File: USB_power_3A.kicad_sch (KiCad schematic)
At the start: 8 parts, among them J14 500SSP1S2M2QEA, J9 USB_C_Receptacle_PowerOnly_6P, U1 USBLC6-2SC6

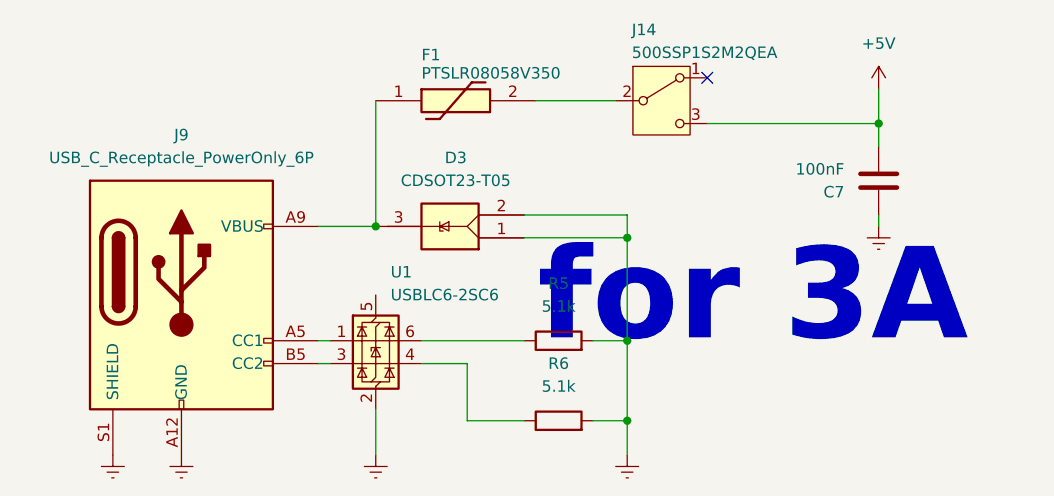
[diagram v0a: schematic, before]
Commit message: annotation and pcb outline
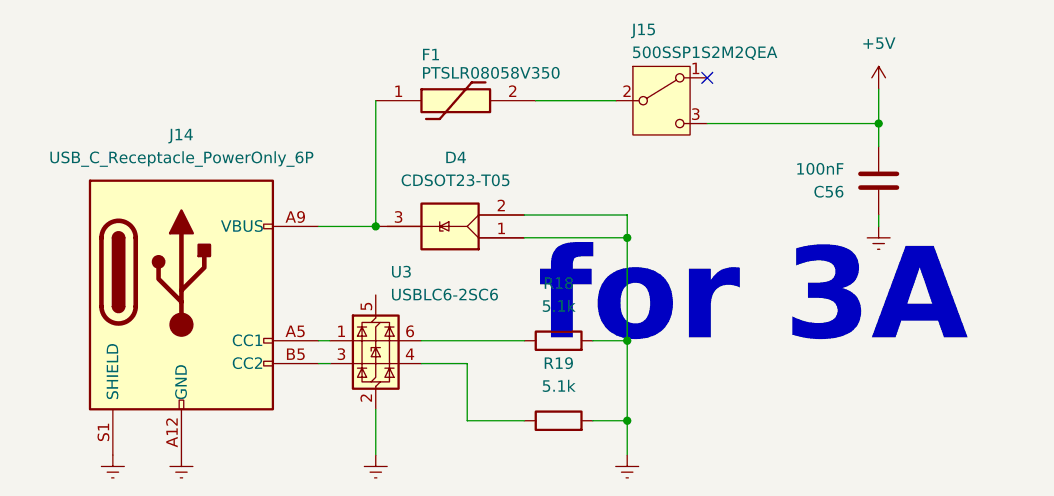
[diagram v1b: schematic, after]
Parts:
- renumbered C7 to C56, D3 to D4, J9 to J14, J14 to J15, R5 to R18, R6 to R19, U1 to U3
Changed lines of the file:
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@@
 		(on_board yes)
 		(dnp no)
-		(property "Reference" "J14"
+		(property "Reference" "J15"
 			(at 169.418 75.946 0)
 			(effects
@@
 			(project "RSC_extension_board"
 				(path "/1f48ed4c-84ce-4e77-88fc-25bf92dcee2d/a313b83a-a07e-4d1d-b36b-94744ea8af4d"
-					(reference "J14")
+					(reference "J15")
 					(unit 1)
 				)
@@
 		(dnp no)
 		(fields_autoplaced yes)
-		(property "Reference" "R6"
+		(property "Reference" "R19"
 			(at 161.29 113.03 90)
 			(effects
@@
 			(project "RSC_extension_board"
 				(path "/1f48ed4c-84ce-4e77-88fc-25bf92dcee2d/a313b83a-a07e-4d1d-b36b-94744ea8af4d"
-					(reference "R6")
+					(reference "R19")
 					(unit 1)
 				)
@@
 		(dnp no)
 		(fields_autoplaced yes)
-		(property "Reference" "#PWR026"
+		(property "Reference" "#PWR082"
 			(at 140.97 129.54 0)
 			(effects
@@
 			(project "RSC_extension_board"
 				(path "/1f48ed4c-84ce-4e77-88fc-25bf92dcee2d/a313b83a-a07e-4d1d-b36b-94744ea8af4d"
-					(reference "#PWR026")
+					(reference "#PWR082")
 					(unit 1)
 				)
@@
 		(dnp no)
 		(fields_autoplaced yes)
-		(property "Reference" "#PWR021"
+		(property "Reference" "#PWR084"
 			(at 196.85 86.36 0)
 			(effects
@@
 			(project "RSC_extension_board"
 				(path "/1f48ed4c-84ce-4e77-88fc-25bf92dcee2d/a313b83a-a07e-4d1d-b36b-94744ea8af4d"
-					(reference "#PWR021")
+					(reference "#PWR084")
 					(unit 1)
 				)
@@
 		(dnp no)
 		(fields_autoplaced yes)
-		(property "Reference" "#PWR74"
+		(property "Reference" "#PWR080"
 			(at 111.76 129.54 0)
 			(effects
@@
 			(project "RSC_extension_board"
 				(path "/1f48ed4c-84ce-4e77-88fc-25bf92dcee2d/a313b83a-a07e-4d1d-b36b-94744ea8af4d"
-					(reference "#PWR74")
+					(reference "#PWR080")
 					(unit 1)
 				)
@@
 		(dnp no)
 		(fields_autoplaced yes)
-		(property "Reference" "R5"
+		(property "Reference" "R18"
 			(at 161.29 104.14 90)
 			(effects
@@
 			(project "RSC_extension_board"
 				(path "/1f48ed4c-84ce-4e77-88fc-25bf92dcee2d/a313b83a-a07e-4d1d-b36b-94744ea8af4d"
-					(reference "R5")
+					(reference "R18")
 					(unit 1)
 				)
@@
 		(dnp no)
 		(fields_autoplaced yes)
-		(property "Reference" "C7"
+		(property "Reference" "C56"
 			(at 193.04 93.9801 0)
 			(effects
@@
 			(project "RSC_extension_board"
 				(path "/1f48ed4c-84ce-4e77-88fc-25bf92dcee2d/a313b83a-a07e-4d1d-b36b-94744ea8af4d"
-					(reference "C7")
+					(reference "C56")
 					(unit 1)
 				)
@@
 		(dnp no)
 		(fields_autoplaced yes)
-		(property "Reference" "U1"
+		(property "Reference" "U3"
 			(at 142.6211 102.87 0)
 			(effects
@@
 			(project "RSC_extension_board"
 				(path "/1f48ed4c-84ce-4e77-88fc-25bf92dcee2d/a313b83a-a07e-4d1d-b36b-94744ea8af4d"
-					(reference "U1")
+					(reference "U3")
 					(unit 1)
 				)
@@
 		(dnp no)
 		(fields_autoplaced yes)
-		(property "Reference" "J9"
+		(property "Reference" "J14"
 			(at 119.38 87.63 0)
 			(effects
@@
 			(project "RSC_extension_board"
 				(path "/1f48ed4c-84ce-4e77-88fc-25bf92dcee2d/a313b83a-a07e-4d1d-b36b-94744ea8af4d"
-					(reference "J9")
+					(reference "J14")
 					(unit 1)
 				)
@@
 		(dnp no)
 		(fields_autoplaced yes)
-		(property "Reference" "#PWR027"
+		(property "Reference" "#PWR083"
 			(at 168.91 129.54 0)
 			(effects
@@
 			(project "RSC_extension_board"
 				(path "/1f48ed4c-84ce-4e77-88fc-25bf92dcee2d/a313b83a-a07e-4d1d-b36b-94744ea8af4d"
-					(reference "#PWR027")
+					(reference "#PWR083")
 					(unit 1)
 				)
@@
 		(dnp no)
 		(fields_autoplaced yes)
-		(property "Reference" "#PWR024"
+		(property "Reference" "#PWR085"
 			(at 196.85 104.14 0)
 			(effects
@@
 			(project "RSC_extension_board"
 				(path "/1f48ed4c-84ce-4e77-88fc-25bf92dcee2d/a313b83a-a07e-4d1d-b36b-94744ea8af4d"
-					(reference "#PWR024")
+					(reference "#PWR085")
 					(unit 1)
 				)
@@
 		(dnp no)
 		(fields_autoplaced yes)
-		(property "Reference" "D3"
+		(property "Reference" "D4"
 			(at 149.86 90.17 0)
 			(effects
@@
 			(project "RSC_extension_board"
 				(path "/1f48ed4c-84ce-4e77-88fc-25bf92dcee2d/a313b83a-a07e-4d1d-b36b-94744ea8af4d"
-					(reference "D3")
+					(reference "D4")
 					(unit 1)
 				)
@@
 		(dnp no)
 		(fields_autoplaced yes)
-		(property "Reference" "#PWR025"
+		(property "Reference" "#PWR081"
 			(at 119.38 129.54 0)
 			(effects
@@
 			(project "RSC_extension_board"
 				(path "/1f48ed4c-84ce-4e77-88fc-25bf92dcee2d/a313b83a-a07e-4d1d-b36b-94744ea8af4d"
-					(reference "#PWR025")
-					(unit 1)
-				)
+					(reference "#PWR081")
+					(unit 1)
+				)
